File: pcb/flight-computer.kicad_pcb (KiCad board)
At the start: 4 copper layers, 83.7 x 62.9 mm, 96 parts, among them J1 MicroSD Slot, J2 USB_C_Receptacle_USB2.0_16P, J3 SMA_Coax, J4 Conn_01x02, J5 ARM, Q1 PMOS, Q2 NMOS, SW1 SW_Push, SW2 SW_Push, U1 RP2040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

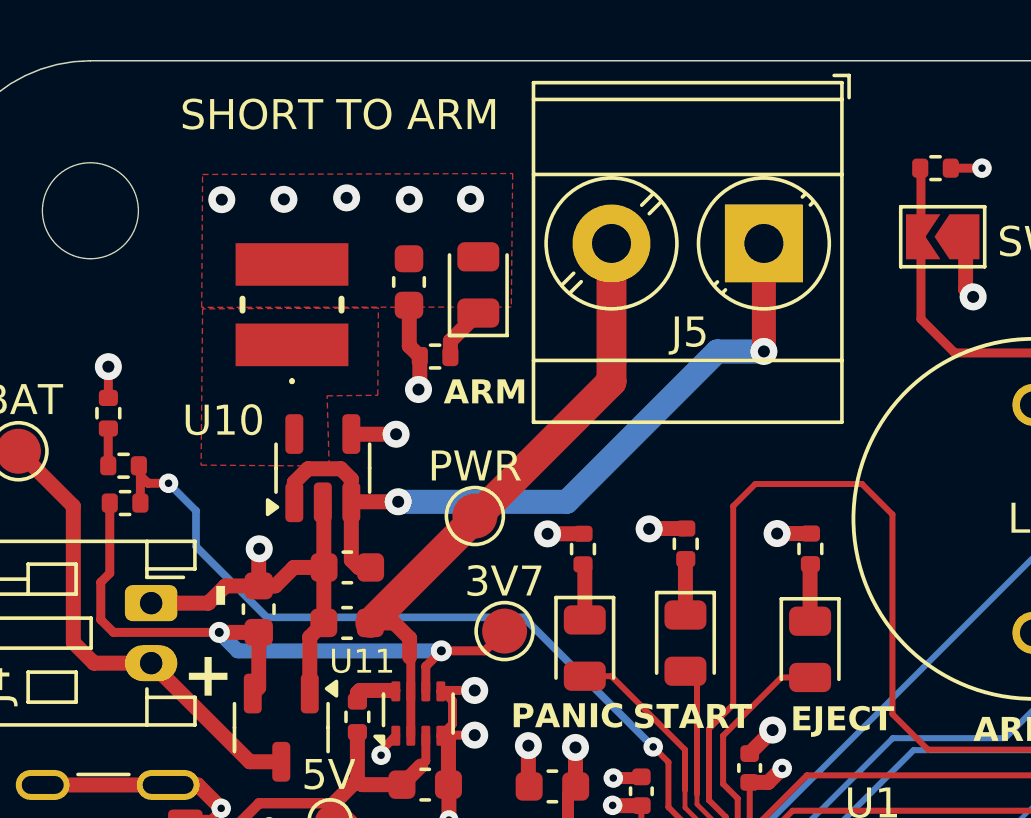
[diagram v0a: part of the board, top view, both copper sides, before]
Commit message: Made terminal block smaller.
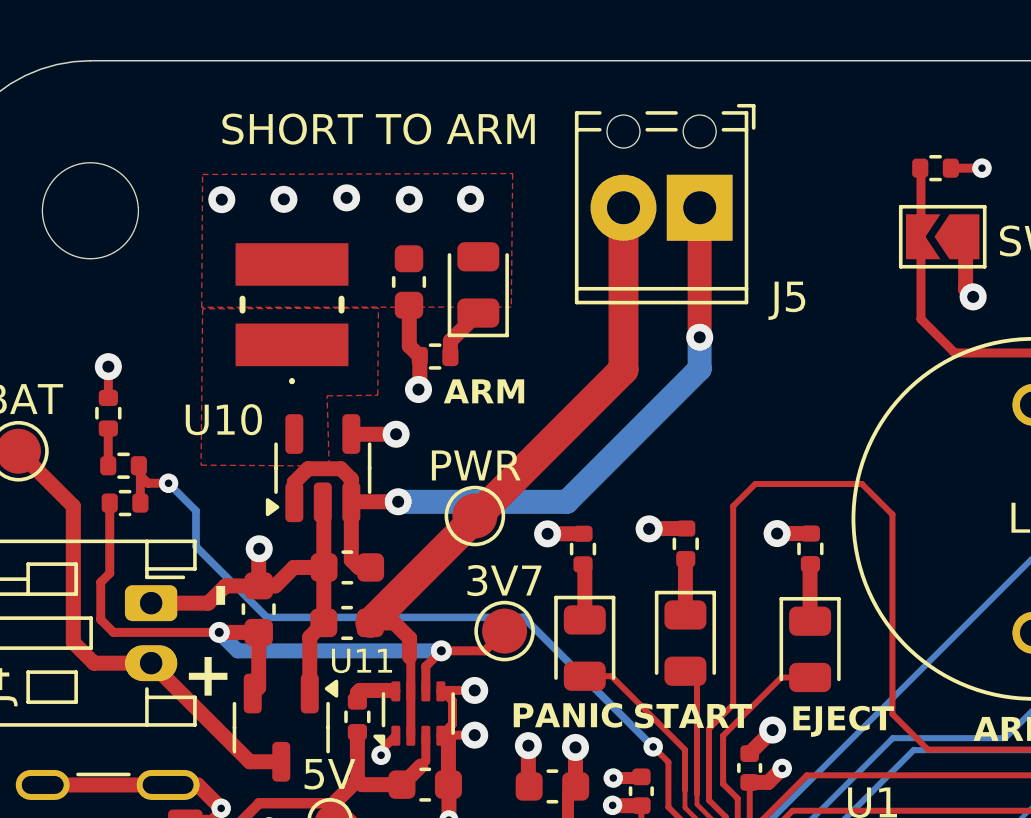
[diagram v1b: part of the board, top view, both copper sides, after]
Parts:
- J5: footprint TerminalBlock_Phoenix:TerminalBlock_Phoenix_MKDS-3-2-5.08_1x02_P5.08mm_Horizontal -> TerminalBlock_Phoenix:TerminalBlock_Phoenix_MPT-0,5-2-2.54_1x02_P2.54mm_Horizontal
- moved J5 2.45 mm to (109.5, 75.5)
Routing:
- net /Power/PWR_SRC: track 20.8 -> 22.1 mm
- net /Power/REGULATOR_IN: track 25.8 -> 25.2 mm
